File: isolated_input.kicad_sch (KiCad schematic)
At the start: 17 parts, among them Q1 PMV213SN, Q2 DMP610DL, Q4 2N7002, Q8 2N7002, U1 EL3H7, U3 AL5809-15P, U5 AL5809-15P, U8 EL3H7

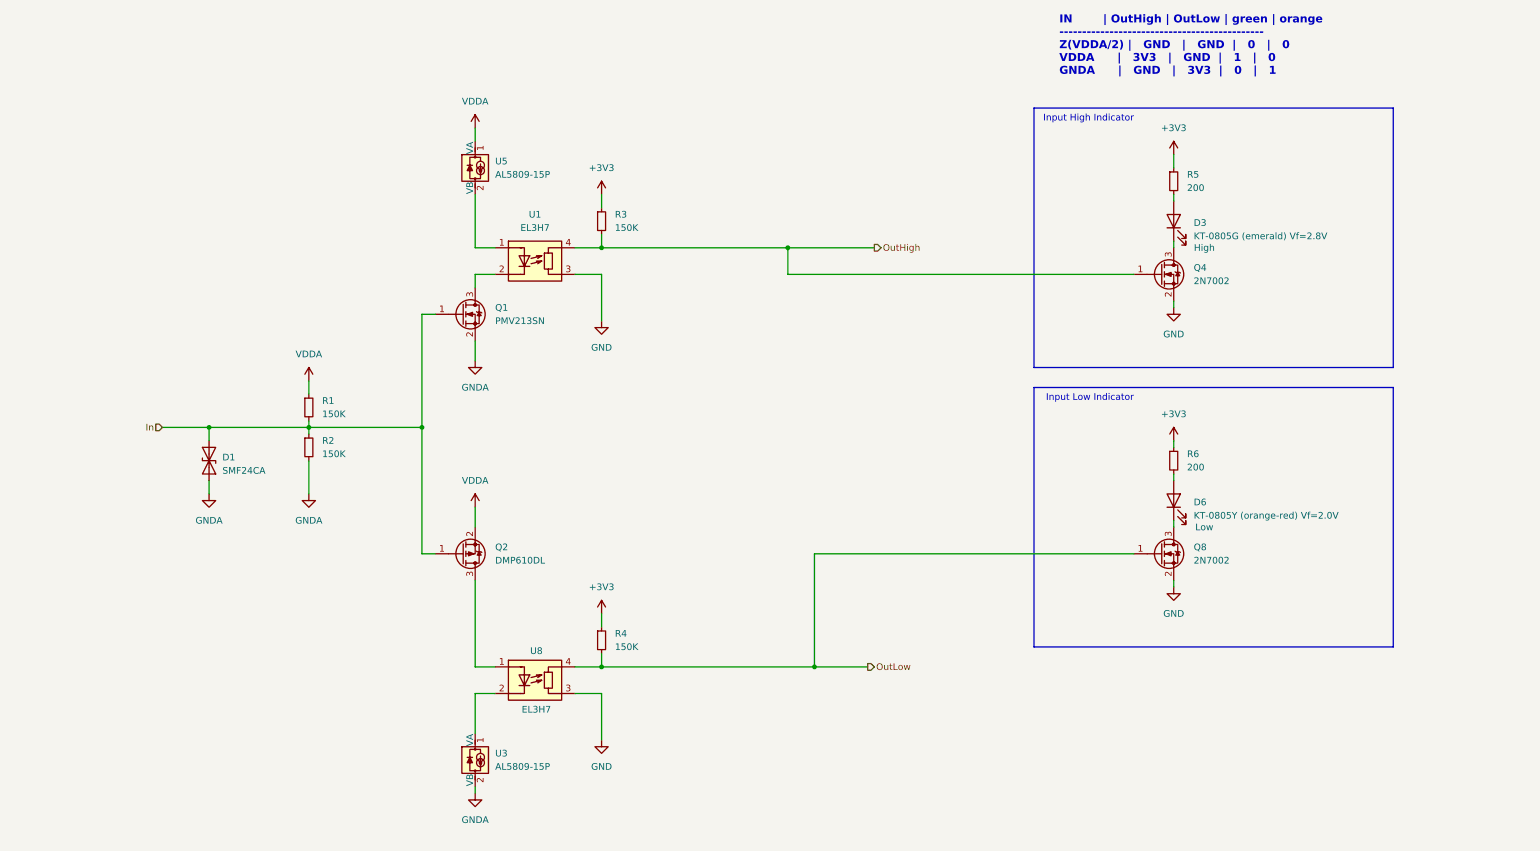
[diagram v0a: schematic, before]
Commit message: Fix constant current source (AL5809) symbol and footprint
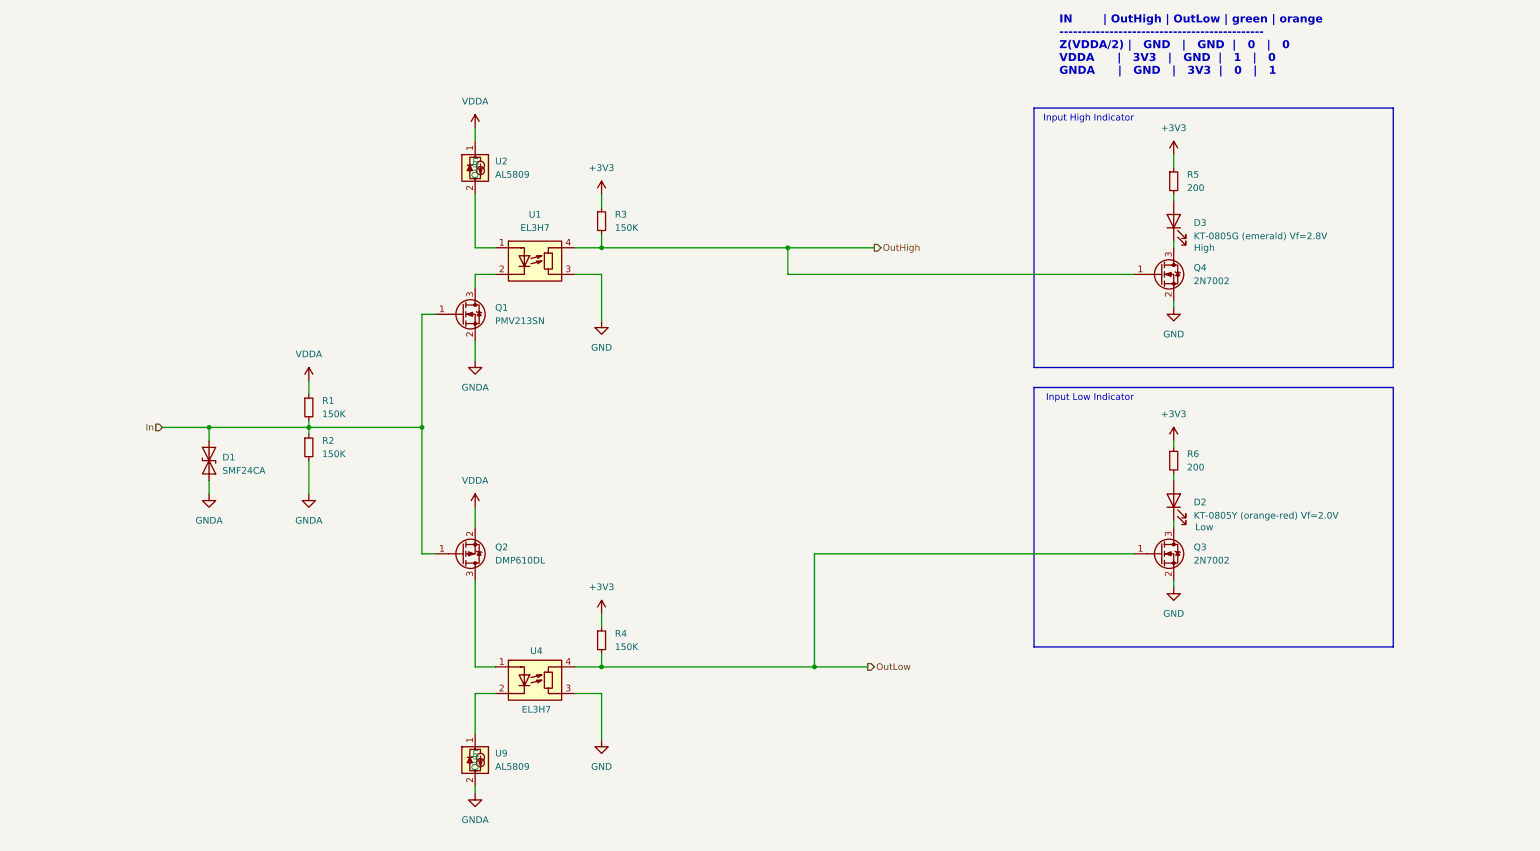
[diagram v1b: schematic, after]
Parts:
- removed U3, U5: AL5809-15P, Diode_SMD:D_PowerDI-123, symbol Driver_LED:CL220K4-G
- added U2, U9: AL5809, lcsc_stuff:PowerDI-123, symbol lcsc_stuff:AL5809
- U1: footprint Package_SO:SSOP-4_4.4x2.6mm_P1.27mm -> lcsc_stuff:SSOP-4_4.4x2.6mm_P1.27mm
- U4: renamed from U8; footprint Package_SO:SSOP-4_4.4x2.6mm_P1.27mm -> lcsc_stuff:SSOP-4_4.4x2.6mm_P1.27mm
- renumbered D6 to D2, Q8 to Q3
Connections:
- net GNDA: now also U9.2 (Out)
- net VDDA: now also U2.1 (in)
- net at U4.2 (K): now also U9.1 (in)
- net at U1.1 (A): now also U2.2 (Out)
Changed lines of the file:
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@@
 	(wire
 		(pts
-			(xy 101.6 165.1) (xy 101.6 166.37)
+			(xy 101.6 166.37) (xy 101.6 165.1)
 		)
 		(stroke
@@
 	)
 	(symbol
-		(lib_id "Driver_LED:CL220K4-G")
-		(at 101.6 160.02 0)
-		(unit 1)
-		(exclude_from_sim no)
-		(in_bom yes)
-		(on_board yes)
-		(dnp no)
-		(fields_autoplaced yes)
-		(property "Reference" "U3"
-			(at 105.41 158.7499 0)
-			(effects
-				(font
-					(size 1.27 1.27)
-				)
-				(justify left)
-			)
-		)
-		(property "Value" "AL5809-15P"
-			(at 105.41 161.2899 0)
-			(effects
-				(font
-					(size 1.27 1.27)
-				)
-				(justify left)
-			)
-		)
-		(property "Footprint" "Diode_SMD:D_PowerDI-123"
-			(at 105.41 161.29 0)
-			(effects
-				(font
-					(size 1.27 1.27)
-				)
-				(justify left)
-				(hide yes)
-			)
-		)
-		(property "Datasheet" "https://www.lcsc.com/datasheet/lcsc_datasheet_2304140030_Diodes-Incorporated-AL5809-15P1-7_C145092.pdf"
-			(at 101.854 160.02 0)
-			(effects
-				(font
-					(size 1.27 1.27)
-				)
-				(hide yes)
-			)
-		)
-		(property "Description" "Temperature Compensated Constant Current LED IC, D-PAK"
-			(at 101.6 160.02 0)
-			(effects
-				(font
-					(size 1.27 1.27)
-				)
-				(hide yes)
-			)
-		)
-		(property "LCSC Part#" "C145092"
-			(at 101.6 160.02 0)
-			(effects
-				(font
-					(size 1.27 1.27)
-				)
-				(hide yes)
-			)
-		)
-		(property "Text" ""
-			(at 101.6 160.02 0)
-			(effects
-				(font
-					(size 1.27 1.27)
-				)
-			)
-		)
-		(pin "2"
-		)
-		(pin "3"
-		)
-		(pin "1"
-		)
-		(instances
-			(project "multi_input_edgy"
-				(path "/6245d815-3a0a-4de6-9134-28f5571821de/2f847f2b-44e1-4b01-8806-4ee445d9979e/036cff62-e137-4ca3-a5ab-ba4d49211600"
-					(reference "U3")
-					(unit 1)
-				)
-				(path "/6245d815-3a0a-4de6-9134-28f5571821de/2f847f2b-44e1-4b01-8806-4ee445d9979e/4c9248e3-5311-42f4-8e48-146a566f42fa"
-					(reference "U6")
-					(unit 1)
-				)
-				(path "/6245d815-3a0a-4de6-9134-28f5571821de/2f847f2b-44e1-4b01-8806-4ee445d9979e/bd25a8d3-cc96-44db-9ab7-a39e0aec573c"
-					(reference "U10")
-					(unit 1)
-				)
-				(path "/6245d815-3a0a-4de6-9134-28f5571821de/2f847f2b-44e1-4b01-8806-4ee445d9979e/e6b33b4e-cb11-4e55-91b7-372c213eef5e"
-					(reference "U14")
-					(unit 1)
-				)
-			)
-		)
-	)
-	(symbol
 		(lib_id "power:GND")
 		(at 125.73 156.21 0)
@@
 	)
 	(symbol
+		(lib_id "lcsc_stuff:AL5809")
+		(at 101.6 152.4 0)
+		(unit 1)
+		(exclude_from_sim no)
+		(in_bom yes)
+		(on_board yes)
+		(dnp no)
+		(fields_autoplaced yes)
+		(property "Reference" "U9"
+			(at 105.41 158.7499 0)
+			(effects
+				(font
+					(size 1.27 1.27)
+				)
+				(justify left)
+			)
+		)
+		(property "Value" "AL5809"
+			(at 105.41 161.2899 0)
+			(effects
+				(font
+					(size 1.27 1.27)
+				)
+				(justify left)
+			)
+		)
+		(property "Footprint" "lcsc_stuff:PowerDI-123"
+			(at 101.346 178.308 0)
+			(effects
+				(font
+					(size 1.27 1.27)
+				)
+				(hide yes)
+			)
+		)
+		(property "Datasheet" "https://www.lcsc.com/datasheet/lcsc_datasheet_2304140030_Diodes-Incorporated-AL5809-15P1-7_C145092.pdf"
+			(at 102.616 180.34 0)
+			(effects
+				(font
+					(size 1.27 1.27)
+				)
+				(hide yes)
+			)
+		)
+		(property "Description" "60V Two Terminal Constant Current LED Driver"
+			(at 101.346 182.372 0)
+			(effects
+				(font
+					(size 1.27 1.27)
+				)
+				(hide yes)
+			)
+		)
+		(property "LCSC Part#" "C145092"
+			(at 102.108 184.658 0)
+			(effects
+				(font
+					(size 1.27 1.27)
+				)
+				(hide yes)
+			)
+		)
+		(pin "1"
+		)
+		(pin "2"
+		)
+		(instances
+			(project ""
+				(path "/6245d815-3a0a-4de6-9134-28f5571821de/2f847f2b-44e1-4b01-8806-4ee445d9979e/036cff62-e137-4ca3-a5ab-ba4d49211600"
+					(reference "U9")
+					(unit 1)
+				)
+				(path "/6245d815-3a0a-4de6-9134-28f5571821de/2f847f2b-44e1-4b01-8806-4ee445d9979e/4c9248e3-5311-42f4-8e48-146a566f42fa"
+					(reference "U10")
+					(unit 1)
+				)
+				(path "/6245d815-3a0a-4de6-9134-28f5571821de/2f847f2b-44e1-4b01-8806-4ee445d9979e/bd25a8d3-cc96-44db-9ab7-a39e0aec573c"
+					(reference "U13")
+					(unit 1)
+				)
+				(path "/6245d815-3a0a-4de6-9134-28f5571821de/2f847f2b-44e1-4b01-8806-4ee445d9979e/e6b33b4e-cb11-4e55-91b7-372c213eef5e"
+					(reference "U14")
+					(unit 1)
+				)
+			)
+		)
+	)
+	(symbol
 		(lib_id "Device:R_Small")
 		(at 234.95 49.53 0)
@@
 		(dnp no)
 		(fields_autoplaced yes)
-		(property "Reference" "Q8"
+		(property "Reference" "Q3"
 			(at 238.76 119.3799 0)
 			(effects
@@
 		(on_board yes)
 		(dnp no)
-		(property "Reference" "U8"
+		(property "Reference" "U4"
 			(at 113.284 139.192 0)
 			(effects
@@
 			)
 		)
-		(property "Footprint" "Package_SO:SSOP-4_4.4x2.6mm_P1.27mm"
+		(property "Footprint" "lcsc_stuff:SSOP-4_4.4x2.6mm_P1.27mm"
 			(at 113.03 152.4 0)
 			(effects
@@
 	)
 	(symbol
-		(lib_id "Driver_LED:CL220K4-G")
-		(at 101.6 46.99 0)
-		(unit 1)
-		(exclude_from_sim no)
-		(in_bom yes)
-		(on_board yes)
-		(dnp no)
-		(fields_autoplaced yes)
-		(property "Reference" "U5"
-			(at 105.41 45.7199 0)
-			(effects
-				(font
-					(size 1.27 1.27)
-				)
-				(justify left)
-			)
-		)
-		(property "Value" "AL5809-15P"
-			(at 105.41 48.2599 0)
-			(effects
-				(font
-					(size 1.27 1.27)
-				)
-				(justify left)
-			)
-		)
-		(property "Footprint" "Diode_SMD:D_PowerDI-123"
-			(at 105.41 48.26 0)
-			(effects
-				(font
-					(size 1.27 1.27)
-				)
-				(justify left)
-				(hide yes)
-			)
-		)
-		(property "Datasheet" "https://www.lcsc.com/datasheet/lcsc_datasheet_2304140030_Diodes-Incorporated-AL5809-15P1-7_C145092.pdf"
-			(at 101.854 46.99 0)
-			(effects
-				(font
-					(size 1.27 1.27)
-				)
-				(hide yes)
-			)
-		)
-		(property "Description" "Temperature Compensated Constant Current LED IC, D-PAK"
-			(at 101.6 46.99 0)
-			(effects
-				(font
-					(size 1.27 1.27)
-				)
-				(hide yes)
-			)
-		)
-		(property "LCSC Part#" "C145092"
-			(at 101.6 46.99 0)
-			(effects
-				(font
-					(size 1.27 1.27)
-				)
-				(hide yes)
-			)
-		)
-		(pin "2"
-		)
-		(pin "3"
-		)
-		(pin "1"
-		)
-		(instances
-			(project "multi_input_edgy"
-				(path "/6245d815-3a0a-4de6-9134-28f5571821de/2f847f2b-44e1-4b01-8806-4ee445d9979e/036cff62-e137-4ca3-a5ab-ba4d49211600"
-					(reference "U2")
-					(unit 1)
-				)
-				(path "/6245d815-3a0a-4de6-9134-28f5571821de/2f847f2b-44e1-4b01-8806-4ee445d9979e/4c9248e3-5311-42f4-8e48-146a566f42fa"
-					(reference "U5")
-					(unit 1)
-				)
-				(path "/6245d815-3a0a-4de6-9134-28f5571821de/2f847f2b-44e1-4b01-8806-4ee445d9979e/bd25a8d3-cc96-44db-9ab7-a39e0aec573c"
-					(reference "U9")
-					(unit 1)
-				)
-				(path "/6245d815-3a0a-4de6-9134-28f5571821de/2f847f2b-44e1-4b01-8806-4ee445d9979e/e6b33b4e-cb11-4e55-91b7-372c213eef5e"
-					(reference "U13")
-					(unit 1)
-				)
-			)
-		)
-	)
-	(symbol
 		(lib_id "Device:R_Small")
 		(at 125.73 137.16 0)
@@
 		(on_board yes)
 		(dnp no)
-		(property "Reference" "D6"
+		(property "Reference" "D2"
 			(at 238.76 110.8074 90)
 			(effects
@@
 			)
 		)
-		(property "Footprint" "Package_SO:SSOP-4_4.4x2.6mm_P1.27mm"
+		(property "Footprint" "lcsc_stuff:SSOP-4_4.4x2.6mm_P1.27mm"
 			(at 113.03 72.39 0)
 			(effects
@@
 			)
 		)
-		(property "Text" ""
-			(at 99.06 120.65 0)
-			(effects
-				(font
-					(size 1.27 1.27)
-				)
-			)
-		)
 		(pin "1"
 		)
@@
 					(unit 1)
 				)
+			)
+		)
+	)
+	(symbol
+		(lib_id "lcsc_stuff:AL5809")
+		(at 101.6 39.37 0)
+		(unit 1)
+		(exclude_from_sim no)
+		(in_bom yes)
+		(on_board yes)
+		(dnp no)
+		(fields_autoplaced yes)
+		(property "Reference" "U2"
+			(at 105.41 45.7199 0)
+			(effects
+				(font
+					(size 1.27 1.27)
+				)
+				(justify left)
+			)
+		)
+		(property "Value" "AL5809"
+			(at 105.41 48.2599 0)
+			(effects
+				(font
+					(size 1.27 1.27)
+				)
+				(justify left)
+			)
+		)
+		(property "Footprint" "lcsc_stuff:PowerDI-123"
+			(at 101.346 65.278 0)
+			(effects
+				(font
+					(size 1.27 1.27)
+				)
+				(hide yes)
+			)
+		)
+		(property "Datasheet" "https://www.lcsc.com/datasheet/lcsc_datasheet_2304140030_Diodes-Incorporated-AL5809-15P1-7_C145092.pdf"
+			(at 102.616 67.31 0)
+			(effects
+				(font
+					(size 1.27 1.27)
+				)
+				(hide yes)
+			)
+		)
+		(property "Description" "60V Two Terminal Constant Current LED Driver"
+			(at 101.346 69.342 0)
+			(effects
+				(font
+					(size 1.27 1.27)
+				)
+				(hide yes)
+			)
+		)
+		(property "LCSC Part#" "C145092"
+			(at 102.108 71.628 0)
+			(effects
+				(font
+					(size 1.27 1.27)
+				)
+				(hide yes)
+			)
+		)
+		(pin "1"
+		)
+		(pin "2"
+		)
+		(instances
+			(project ""
+				(path "/6245d815-3a0a-4de6-9134-28f5571821de/2f847f2b-44e1-4b01-8806-4ee445d9979e/036cff62-e137-4ca3-a5ab-ba4d49211600"
+					(reference "U2")
+					(unit 1)
+				)
+				(path "/6245d815-3a0a-4de6-9134-28f5571821de/2f847f2b-44e1-4b01-8806-4ee445d9979e/4c9248e3-5311-42f4-8e48-146a566f42fa"
+					(reference "U3")
+					(unit 1)
+				)
+				(path "/6245d815-3a0a-4de6-9134-28f5571821de/2f847f2b-44e1-4b01-8806-4ee445d9979e/bd25a8d3-cc96-44db-9ab7-a39e0aec573c"
+					(reference "U5")
+					(unit 1)
+				)
+				(path "/6245d815-3a0a-4de6-9134-28f5571821de/2f847f2b-44e1-4b01-8806-4ee445d9979e/e6b33b4e-cb11-4e55-91b7-372c213eef5e"
+					(reference "U6")
+					(unit 1)
+				)

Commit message: Get board name and version from text variable
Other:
- title: (none) -> ${BoardName}
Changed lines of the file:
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@@
 	(generator_version "8.99")
 	(paper "A4")
+	(title_block
+		(title "${BoardName}")
+		(date "2024-11-11")
+		(rev "${Version}")
+	)
 	(rectangle
 		(start 208.28 88.9)

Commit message: Change optocouplers, improve power routing
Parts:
- removed Q3, Q4: 2N7002, Package_TO_SOT_SMD:SOT-23, symbol Transistor_FET:2N7002
- removed R5: 200, Resistor_SMD:R_0402_1005Metric_Pad0.72x0.64mm_HandSolder, symbol Device:R_Small
- removed U2, U9: AL5809, lcsc_stuff:PowerDI-123, symbol lcsc_stuff:AL5809
- added J3: - ${SHEETNAME} +, Connector_TE-Connectivity:TE_826576-3_1x03_P3.96mm_Vertical, symbol Connector:Screw_Terminal_01x03
- added Q3: 2N7002DW, Package_TO_SOT_SMD:SOT-363_SC-70-6, symbol Transistor_FET:FDG6335N
- added R6: 470, Resistor_SMD:R_0402_1005Metric_Pad0.72x0.64mm_HandSolder, symbol Device:R_Small
- R7: renamed from R6; value 200 -> 470; LCSC Part# C25087 -> C25117
- renumbered R1 to R2, R2 to R3, R3 to R4, R4 to R5, U1 to U3
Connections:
- net +3V3: now also R6.1
- net GND: now also Q3.1 (S), Q3.4 (S)
- net GNDA: now also U4.2 (K)
- net VDDA: no longer Q2.2 (S)
- net at D3.2 (A): now also R7.2
- net at D2.1 (K): now also Q3.6 (D)
- net at D3.1 (K): now also Q3.3 (D)
- net at D2.2 (A): now also R6.2; no longer R7.2
- net +1V: now reaches U3.1 (A)
- net +1V: now also Q2.2 (S)
- net In: no longer names the net of D1.2 (A2), Q1.1 (G), Q2.1 (G), R2.2, R3.1
- net In: now also J3.2 (Pin_2)
- net OutHigh renamed ${SHEETNAME}_low
- net ${SHEETNAME}_low: now also Q3.2 (G)
- net OutLow renamed ${SHEETNAME}_high
- net ${SHEETNAME}_high: now also Q3.5 (G)
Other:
- note removed: "IN | OutHigh | OutLow | green | orange --------------------------------------------- Z(VDDA/2) | GND | GND | 0 | 0 VDDA | 3V3 | GND | 1 | 0 GNDA | GND | 3V3 | 0 | 1"
- note removed: "Input High Indicator"
- note removed: "Input Low Indicator"
- title: ${BoardName} -> (none)
- moved on the sheet: D1, D2, D3, Q1, Q2, R2, R3, R4, R5, R7, U3, U4
